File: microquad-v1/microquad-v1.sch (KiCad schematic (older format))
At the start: 6 parts

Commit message: Joe fixed merge
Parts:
- added SW?: SWITCH, symbol SW_DPDT_x2
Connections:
- wire segments 20 -> 23
- no-connect marks 0 -> 1
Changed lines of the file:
@@
 F6 "INT" I R 3550 1550 60
 $EndSheet
+$Comp
+L SW_DPDT_x2 SW?
+U 1 1 59F60CDA
+P 3450 3100
+F 0 "SW?" H 3450 3270 50  0000 C CNN
+F 1 "SWITCH" H 3450 2900 50  0000 C CNN
+F 2 "" H 3450 3100 50  0001 C CNN
+F 3 "" H 3450 3100 50  0001 C CNN
+	1    3450 3100
+	0    1    1    0
+$EndComp
+Wire Wire Line
+	3350 3400 3350 3300
+Wire Wire Line
+	3450 2900 3450 2700
+Wire Wire Line
+	3450 2700 3500 2700
+NoConn ~ 3550 3300
 $Sheet
 S 3900 1000 550  300

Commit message: Double checked and hooked up connections for BLE Added Power and Pin 12 LED
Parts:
- added SW? (x2): Switch, symbol SW_DPDT_x2
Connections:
- wire segments 23 -> 35
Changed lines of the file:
@@
 $Descr A4 11693 8268
 encoding utf-8
-Sheet 1 7
+Sheet 1 8
 Title ""
 Date ""
@@
 $EndSheet
 $Sheet
-S 1125 2300 825  500
+S 725  2300 825  500
 U 59F242F1
 F0 "USB interface" 60
 F1 "usb_uart.sch" 60
-F2 "RX" I R 1950 2450 60
-F3 "TX" I R 1950 2350 60
-F4 "5V" I R 1950 2750 60
+F2 "RX" I R 1550 2450 60
+F3 "TX" I R 1550 2350 60
+F4 "5V" I R 1550 2750 60
 $EndSheet
 $Sheet
@@
 	0    1    1    0
 $EndComp
-Wire Wire Line
-	1950 2350 2300 2350
-Wire Wire Line
-	2300 2350 2300 2250
-Wire Wire Line
-	2300 2250 2450 2250
-Wire Wire Line
-	2450 2350 2400 2350
-Wire Wire Line
-	2400 2350 2400 2450
-Wire Wire Line
-	2400 2450 1950 2450
 $Comp
 L C C?
@@
 $EndSheet
 Wire Wire Line
-	1950 2750 2100 2750
+	1550 2750 2100 2750
 Wire Wire Line
 	2100 2750 2100 3400
@@
 NoConn ~ 3550 3300
 $Sheet
-S 3900 1000 550  300
+S 1006 1650 550  300
 U 59F5C47F
 F0 "BLE" 60
 F1 "ble.sch" 60
-F2 "RX" I L 3900 1100 60
-F3 "TX" I L 3900 1200 60
-$EndSheet
+F2 "RX" I R 1556 1750 60
+F3 "TX" I R 1556 1850 60
+$EndSheet
+$Comp
+L SW_DPDT_x2 SW?
+U 1 1 59F65B2F
+P 2200 2050
+F 0 "SW?" H 2200 2220 50  0000 C CNN
+F 1 "Switch" H 2200 1850 50  0000 C CNN
+F 2 "" H 2200 2050 50  0001 C CNN
+F 3 "" H 2200 2050 50  0001 C CNN
+	1    2200 2050
+	-1   0    0    1
+$EndComp
+$Comp
+L SW_DPDT_x2 SW?
+U 2 1 59F65CBE
+P 2200 2550
+F 0 "SW?" H 2200 2720 50  0000 C CNN
+F 1 "Switch" H 2200 2350 50  0000 C CNN
+F 2 "" H 2200 2550 50  0001 C CNN
+F 3 "" H 2200 2550 50  0001 C CNN
+	2    2200 2550
+	-1   0    0    1
+$EndComp
+Wire Wire Line
+	2400 2550 2450 2550
+Wire Wire Line
+	2450 2550 2450 2350
+Wire Wire Line
+	2400 2050 2450 2050
+Wire Wire Line
+	2450 2050 2450 2250
+Wire Wire Line
+	2000 2650 1800 2650
+Wire Wire Line
+	1800 2650 1800 2350
+Wire Wire Line
+	1800 2350 1550 2350
+Wire Wire Line
+	2000 2150 1700 2150
+Wire Wire Line
+	1700 2150 1700 2450
+Wire Wire Line
+	1700 2450 1550 2450
+Wire Wire Line
+	2000 2450 1850 2450
+Wire Wire Line
+	1850 2450 1850 1850
+Wire Wire Line
+	1850 1850 1550 1850
+Wire Wire Line
+	2000 1950 1900 1950
+Wire Wire Line
+	1900 1950 1900 1750
+Wire Wire Line
+	1900 1750 1550 1750
+$Sheet
+S 6250 4100 500  150
+U 59F67295
+F0 "PowerLED" 60
+F1 "LED.sch" 60
+F2 "Vin" I L 6250 4150 60
+$EndSheet
+$Sheet
+S 6400 3350 500  150
+U 59F67B63
+F0 "Pin12LED" 60
+F1 "LED.sch" 60
+F2 "Vin" I L 6400 3400 60
+$EndSheet
+$Comp
+L +3V3 #PWR?
+U 1 1 59F67E12
+P 6050 4150
+F 0 "#PWR?" H 6050 4000 50  0001 C CNN
+F 1 "+3V3" H 6050 4290 50  0000 C CNN
+F 2 "" H 6050 4150 50  0001 C CNN
+F 3 "" H 6050 4150 50  0001 C CNN
+	1    6050 4150
+	1    0    0    -1
+$EndComp
+Wire Wire Line
+	6050 4150 6250 4150
+Wire Wire Line
+	6150 3400 6400 3400
 $EndSCHEMATC

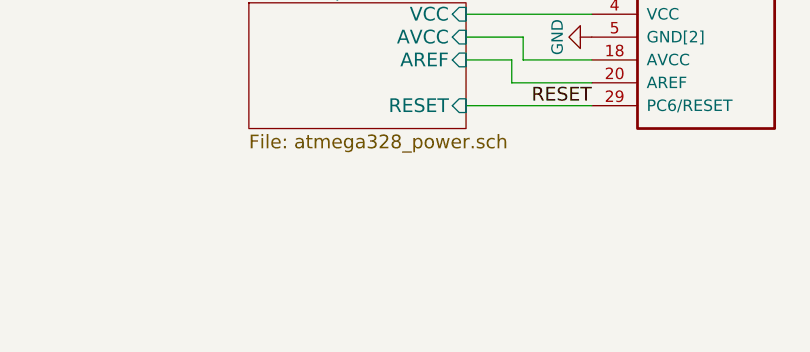
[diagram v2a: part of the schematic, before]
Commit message: Add new battery sub-schematic with new battery charger MCP73812
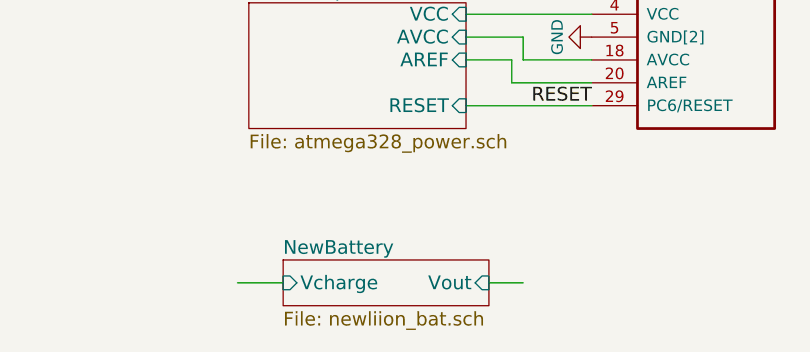
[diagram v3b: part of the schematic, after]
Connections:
- wire segments 35 -> 37
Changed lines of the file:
@@
 $Descr A4 11693 8268
 encoding utf-8
-Sheet 1 8
+Sheet 1 10
 Title ""
 Date ""
@@
 Wire Wire Line
 	6150 3400 6400 3400
+$Sheet
+S 2800 5625 900  200
+U 59F6680F
+F0 "NewBattery" 60
+F1 "newliion_bat.sch" 60
+F2 "Vout" I R 3700 5725 60
+F3 "Vcharge" I L 2800 5725 60
+$EndSheet
+Wire Wire Line
+	3700 5725 3850 5725
+Wire Wire Line
+	2600 5725 2800 5725
 $EndSCHEMATC
